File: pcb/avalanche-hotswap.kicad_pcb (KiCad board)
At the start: 2 copper layers, 173 x 137.5 mm, 140 parts, among them J1 TRRS, J3 OLED, P1 i2c_pin, P2 i2c_pin, SW0 SW_Push, SW1 SW_Push, SW10 SW_Push, SW11 SW_Push, SW12 SW_Push, SW13 SW_Push, SW14 SW_Push, SW15 SW_Push, SW16 SW_Push, SW17 SW_Push, SW18 SW_Push, SW2 SW_Push, SW20 SW_Push, SW21 SW_Push, SW22 SW_Push, SW23 SW_Push, SW24 SW_Push, SW25 SW_Push, SW26 SW_Push, SW27 SW_Push, SW28 SW_Push, SW29 SW_Push, SW3 SW_Push, SW30 SW_Push, SW31 SW_Push, SW32 SW_Push, SW4 SW_Push, SW5 SW_Push, SW6 SW_Push, SW7 SW_Push, SW8 SW_Push, SW9 SW_Push, U1 ProMicro

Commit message: Work in progress
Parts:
- moved D32 3.28 mm to (199.9, 152.7), turned to 217.5 degrees
- moved SW32 2.96 mm to (207.0, 137.1), turned to 127.5 degrees
- moved L9 2.81 mm to (203.2, 140.0), turned to 127.5 degrees
- moved L9 2.66 mm to (195.6, 145.9), turned to 307.5 degrees
- moved SW32 2.66 mm to (191.9, 148.7), turned to 307.5 degrees
- moved D32 2.25 mm to (199.0, 133.2), turned to 37.5 degrees
- moved HM1 1.79 mm to (192.0, 133.6), turned to 340.5 degrees
- moved D31 1.70 mm to (187.1, 135.0), turned to 231 degrees
- moved D26 1.58 mm to (181.3, 114.3), turned to 51 degrees
- moved SW29 1.44 mm to (139.2, 115.5)
- moved ENC3 1.44 mm to (118.4, 113.3)
- moved L29 1.44 mm to (118.4, 108.6)
- moved SW28 1.44 mm to (118.4, 113.3)
- moved D29 1.44 mm to (148.8, 112.3)
- moved HM13 1.44 mm to (129.8, 104.8)
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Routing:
- net row4: track 82.3 -> 70.7 mm
- net encA: track 21.4 -> 33.0 mm
- net Net-(L5-Pad2): track 27.8 -> 28.6 mm
- net row3: track 97.8 -> 97.0 mm, vias 2 -> 3
- net GND: vias 71 -> 70
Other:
- board size 173 x 137.5 mm -> 173 x 138.9 mm

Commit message: WIP
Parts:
- moved HM14 8.24 mm to (212.9, 112.7)
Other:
- outline, holes or cut-outs redrawn

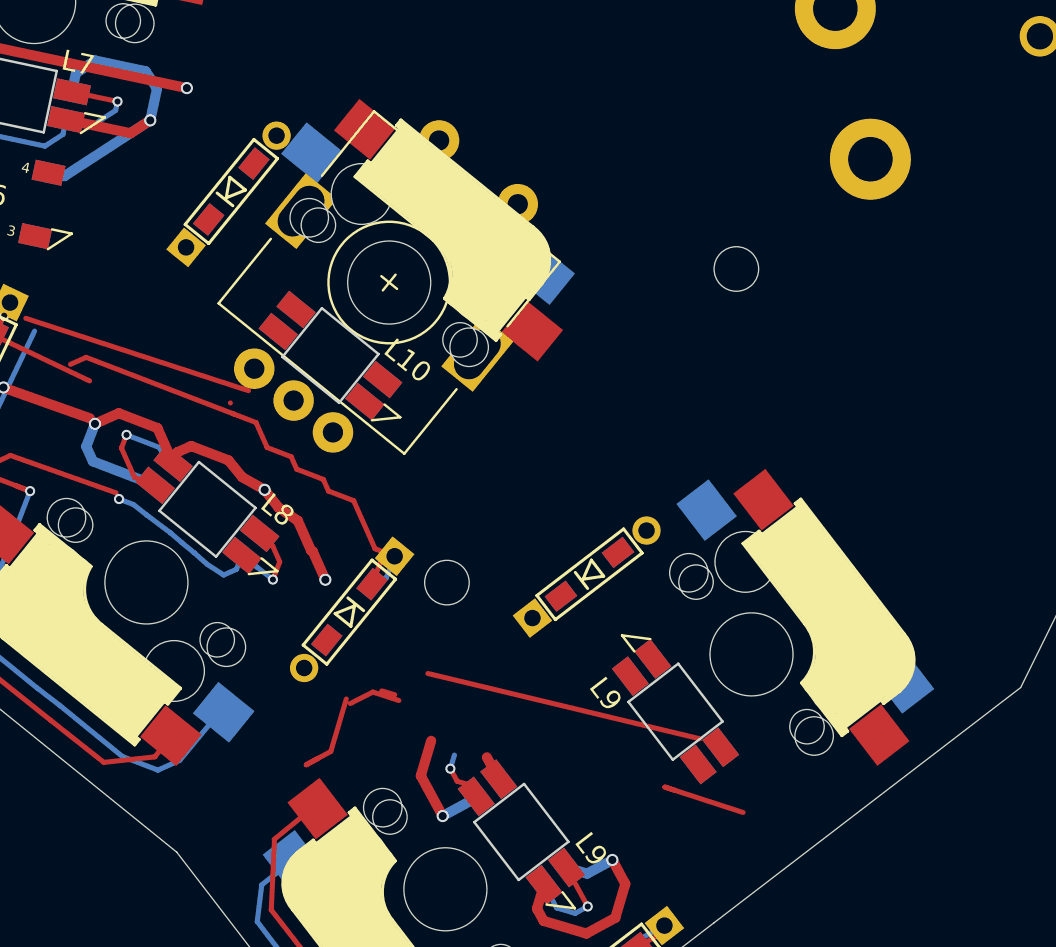
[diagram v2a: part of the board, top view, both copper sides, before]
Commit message: Updated pcb design to the sch
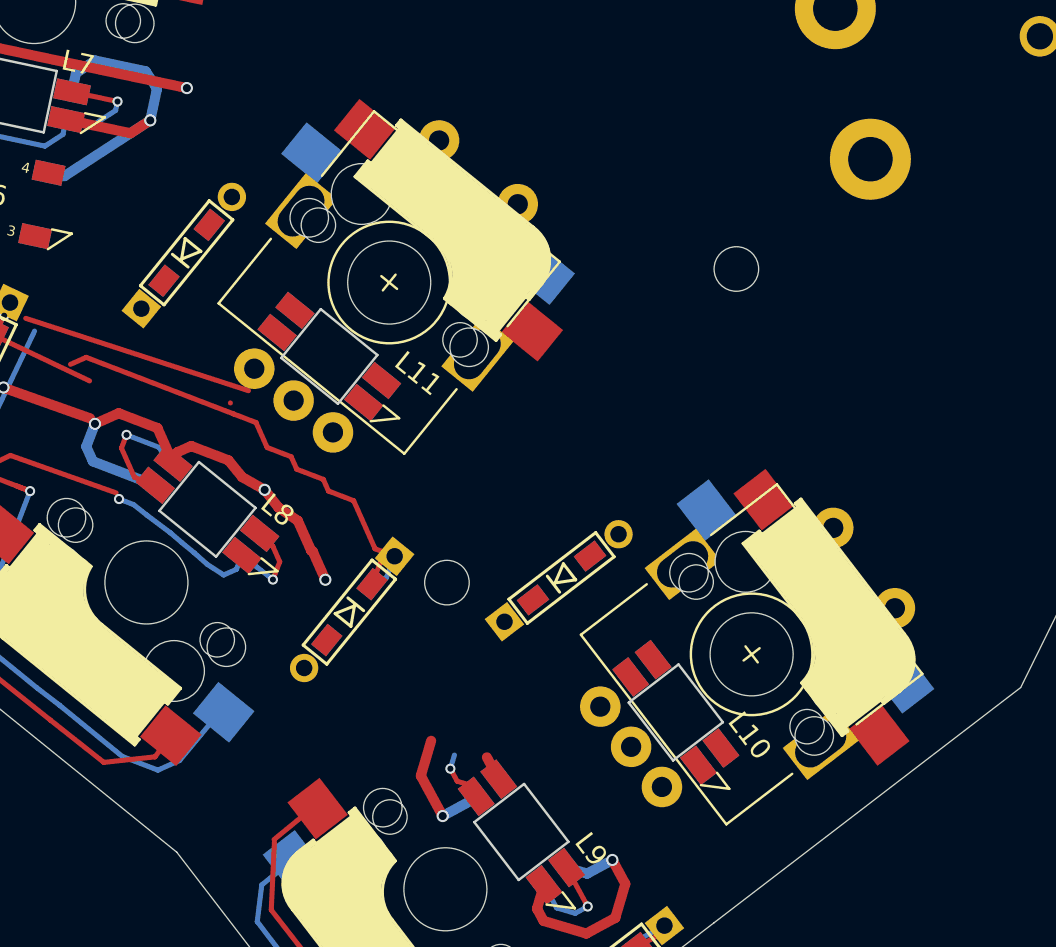
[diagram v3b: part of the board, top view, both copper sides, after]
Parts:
- removed the D32 at (199.0, 133.2)
- removed the L9 at (203.2, 140.0)
- removed the SW32 at (207.0, 137.1)
- added D19: 1N4148, used_footprints:diode_TH_SMD, F.Cu at (197.6, 133.3)
- added ENC1: Rotary_Encoder_Switch, used_footprints:RotaryEncoder_Alps_EC11E-Switch_Vertical_H20mm-keebio_modified, F.Cu at (207.0, 137.1)
- added L11: SK6812MINI_LED, used_footprints:YS-SK6812MINI-E, F.Cu at (186.2, 122.4)
- added SW19: SW_Push, used_footprints:CherryMX_MidHeight_Hotswap_1u, F.Cu at (207.0, 137.1)
- moved L10 24.5 mm to (203.3, 140.0), turned to 307.5 degrees
- moved D26 3.75 mm to (179.1, 117.3)
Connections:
- L12 pad 4: Net-(L10-Pad2) -> Net-(L11-Pad2)
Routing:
- net (no net): track 19.1 -> 0.00 mm
- net col5: track 196.9 -> 189.6 mm
- net Net-(L11-Pad2): track 0.00 -> 4.55 mm, vias 0 -> 1
- net Net-(L10-Pad2): track 4.55 -> 0.00 mm, vias 1 -> 0

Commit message: WIP
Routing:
- net encA: track 33.0 -> 21.4 mm
- net GND: track 984.9 -> 974.7 mm, vias 70 -> 69
- net col0: track 251.2 -> 248.8 mm
- net col5: track 189.6 -> 187.2 mm
- net Net-(L7-Pad2): track 35.2 -> 33.2 mm
- net Net-(L10-Pad4): track 3.93 -> 2.01 mm
- net Net-(L5-Pad2): track 28.6 -> 26.8 mm
- net VCC: track 855.9 -> 854.7 mm
- net sw28r: track 46.4 -> 45.5 mm
- net row4: track 70.7 -> 69.9 mm
- net row1: track 181.4 -> 180.7 mm
- net row3: track 97.0 -> 96.9 mm, vias 3 -> 2

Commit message: WIP
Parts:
- added L6: SK6812MINI_LED, used_footprints:LED_WS2812B_PLCC4_5.0x5.0mm_P3.2mm, F.Cu at (192.1, 133.8)
- moved HM1 29.0 mm to (218.2, 121.3)
- moved D28 14.1 mm to (127.4, 114.0), turned to 270 degrees
- moved HM4 6.47 mm to (154.6, 109.1)
- moved D31 5.89 mm to (183.7, 139.8)
- moved D26 5.86 mm to (182.5, 112.5)
- moved D19 5.85 mm to (202.1, 129.5)
- moved D29 5.85 mm to (147.9, 118.0)
- moved D30 4.25 mm to (167.1, 126.8)
- moved D32 0.37 mm to (199.9, 152.3)
- renumbered L1 to L0, L2 to L1, L11 to L10, L7 to L11, L3 to L2, L4 to L3, L5 to L4, L6 to L5, L8 to L7, L9 to L8, L10 to L9
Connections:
- L10 pad 2: Net-(L11-Pad2) -> Net-(L10-Pad2)
- L11 pad 2: Net-(L7-Pad2) (its old number) -> Net-(L11-Pad2)
- L11 pad 4: ledA -> Net-(L10-Pad2)
- L5 pad 2: ledA -> Net-(L5-Pad2)
- L7 pad 4: Net-(L7-Pad2) (its old number) -> ledA
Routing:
- net GND: track 974.7 -> 940.3 mm
- net Net-(L7-Pad2) (its old number): track 33.2 -> 0.00 mm, vias 4 -> 0
- net sw28r: track 45.5 -> 13.0 mm, vias 1 -> 0
- net row4: track 69.9 -> 38.0 mm, vias 1 -> 0
- net row1: track 180.7 -> 156.0 mm, vias 3 -> 1
- net Net-(D29-Pad2): track 34.9 -> 10.6 mm, vias 1 -> 0
- net Net-(D32-Pad2): track 27.6 -> 3.74 mm, vias 1 -> 0
- net Net-(L19-Pad2): track 37.0 -> 19.0 mm, vias 3 -> 2
- net col4: track 172.6 -> 156.1 mm, vias 7 -> 6
- net col5: track 187.2 -> 173.1 mm, vias 10 -> 8
- net VCC: track 854.7 -> 844.2 mm, vias 52 -> 50
- net ledA: track 12.2 -> 4.71 mm
- net Net-(L11-Pad2): track 4.55 -> 11.5 mm, vias 1 -> 2
- net row3: track 96.9 -> 90.4 mm
- net Net-(D30-Pad2): track 29.1 -> 22.8 mm
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
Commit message: WIP
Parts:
- moved HM3 15.1 mm to (196.3, 129.4)
- moved SW0 11.5 mm to (221.2, 114.9)
- moved W1 3.29 mm to (197.6, 92.6)
- moved HM4 3.00 mm to (152.0, 110.7)
- moved HM13 1.10 mm to (129.6, 105.9)
- moved P2 1.03 mm to (197.6, 90.1)
- moved R1 1.03 mm to (194.8, 84.3)
- moved R2 1.03 mm to (197.6, 84.3)
- moved P1 1.03 mm to (194.8, 90.1)
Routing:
- net Net-(J3-Pad3): track 3.80 -> 0.08 mm
- net Net-(J3-Pad4): track 3.80 -> 0.08 mm
- net Net-(J3-Pad1): track 3.80 -> 0.08 mm
- net Net-(J3-Pad2): track 3.80 -> 0.08 mm
- net Net-(J1-Pad3): track 2.78 -> 0.35 mm
- net VCC: track 844.2 -> 843.4 mm

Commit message: WIP
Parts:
- moved HM14 46.0 mm to (249.2, 84.5)
- moved H16 34.4 mm to (192.4, 64.1)
- moved HM12 23.2 mm to (199.4, 78.3)
- moved SW0 16.5 mm to (232.6, 102.9)
- moved HM1 9.83 mm to (209.9, 116.0)
- moved H15 9.25 mm to (219.8, 108.3)
- moved HM3 8.17 mm to (190.5, 135.2)
- moved R1 4.80 mm to (190.0, 84.0)
- moved W1 4.80 mm to (192.8, 92.3)
- moved P1 4.80 mm to (190.0, 89.8)
- moved P2 4.80 mm to (192.8, 89.8)
- moved R2 4.80 mm to (192.8, 84.0)
- moved L6 3.50 mm to (194.5, 131.3)
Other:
- outline, holes or cut-outs redrawn

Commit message: WIP
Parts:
- moved H16 24.1 mm to (199.3, 87.2)
- moved SW0 11.8 mm to (221.6, 107.1)
- moved H15 7.84 mm to (213.3, 104.0)
- moved W1 7.48 mm to (192.5, 99.7)
- moved D19 6.19 mm to (206.1, 124.8)
- moved P2 5.89 mm to (192.4, 95.7)
- moved R2 5.89 mm to (192.4, 89.9)
- moved P1 5.89 mm to (189.6, 95.7)
- moved R1 5.89 mm to (189.6, 89.9)
- moved J1 0.15 mm to (199.8, 62.2)
- moved L6 0.09 mm to (194.6, 131.3)
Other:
- board size 173 x 138.9 mm -> 173.5 x 138.9 mm
